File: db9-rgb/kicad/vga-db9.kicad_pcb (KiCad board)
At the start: 2 copper layers, 95 x 75 mm, 67 parts, among them J1 Conn_01x03, J2 Conn_01x03, J9 Conn_01x09

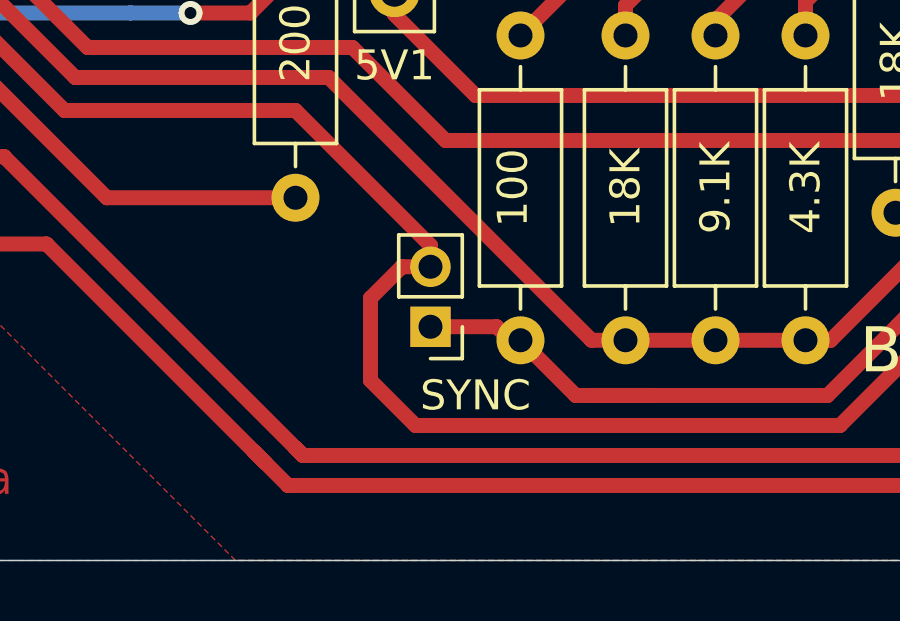
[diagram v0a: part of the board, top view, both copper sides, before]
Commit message: fix JP1 size
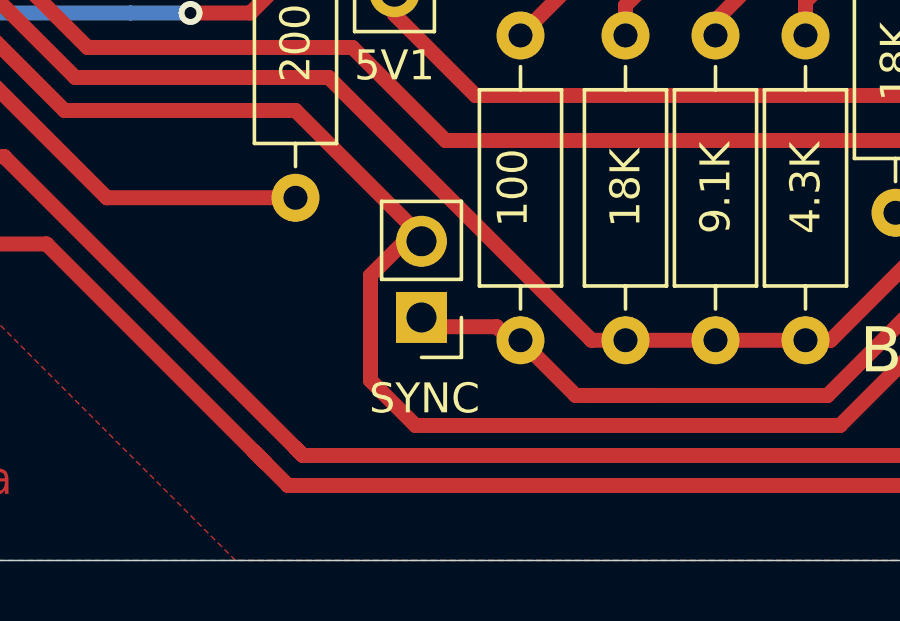
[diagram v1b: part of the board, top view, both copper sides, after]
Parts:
- JP1: footprint Connector_PinHeader_2.00mm:PinHeader_1x02_P2.00mm_Vertical -> Connector_PinHeader_2.54mm:PinHeader_1x02_P2.54mm_Vertical
- moved JP1 0.43 mm to (144.7, 121.9)
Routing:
- net Net-(HSYNC1-Pad2): track 156.5 -> 157.0 mm

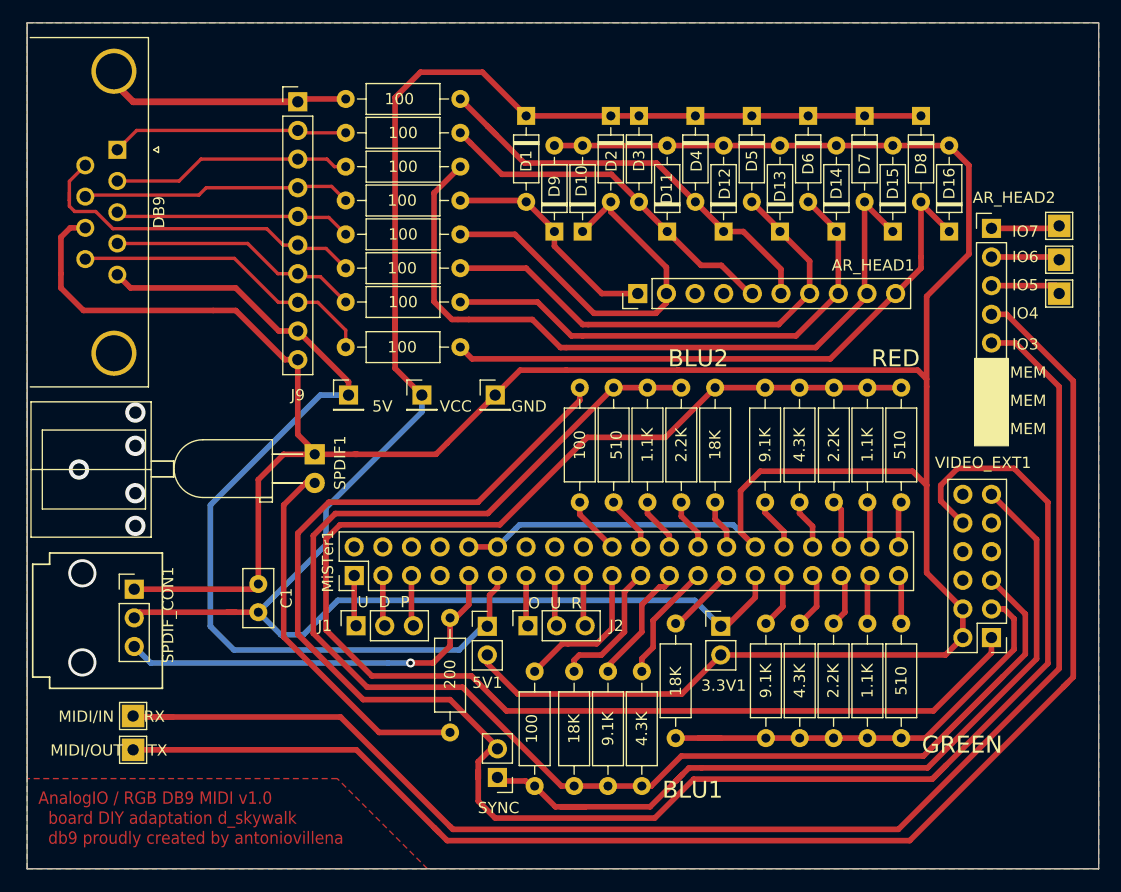
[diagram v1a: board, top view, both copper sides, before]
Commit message: update sync / new tv switch connector
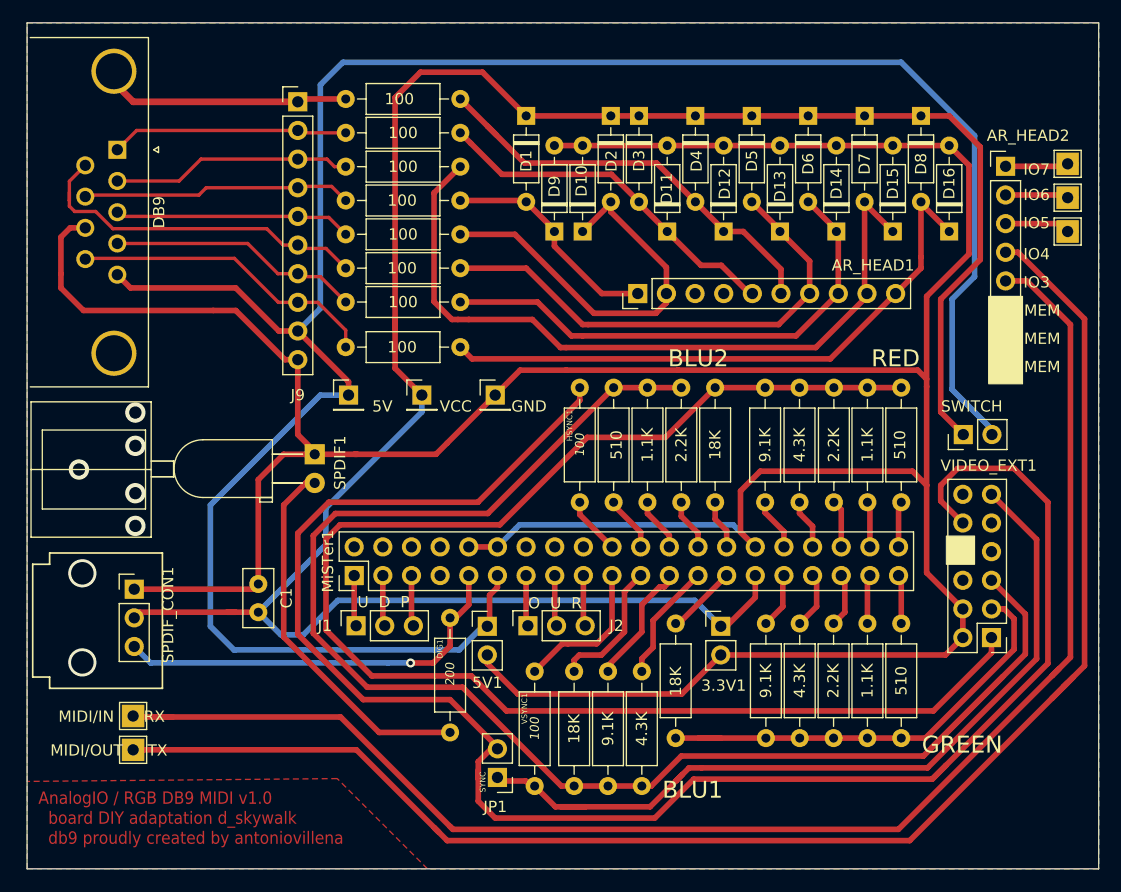
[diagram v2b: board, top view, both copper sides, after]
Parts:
- added SWITCH: PinHeader_1x02_P2.54mm_Vertical, Connector_PinHeader_2.54mm:PinHeader_1x02_P2.54mm_Vertical, F.Cu at (186.0, 91.5)
- moved AR_HEAD2 5.64 mm to (189.8, 67.7)
- moved I2S 5.55 mm to (195.2, 73.5)
- moved I2S 5.55 mm to (195.2, 70.5)
- moved I2S 5.55 mm to (195.2, 67.5)
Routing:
- net 5V: track 83.4 -> 196.4 mm
- net VCC: track 164.4 -> 198.6 mm
- net (no net): track 276.4 -> 291.8 mm

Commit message: fixed resistors and spdif.
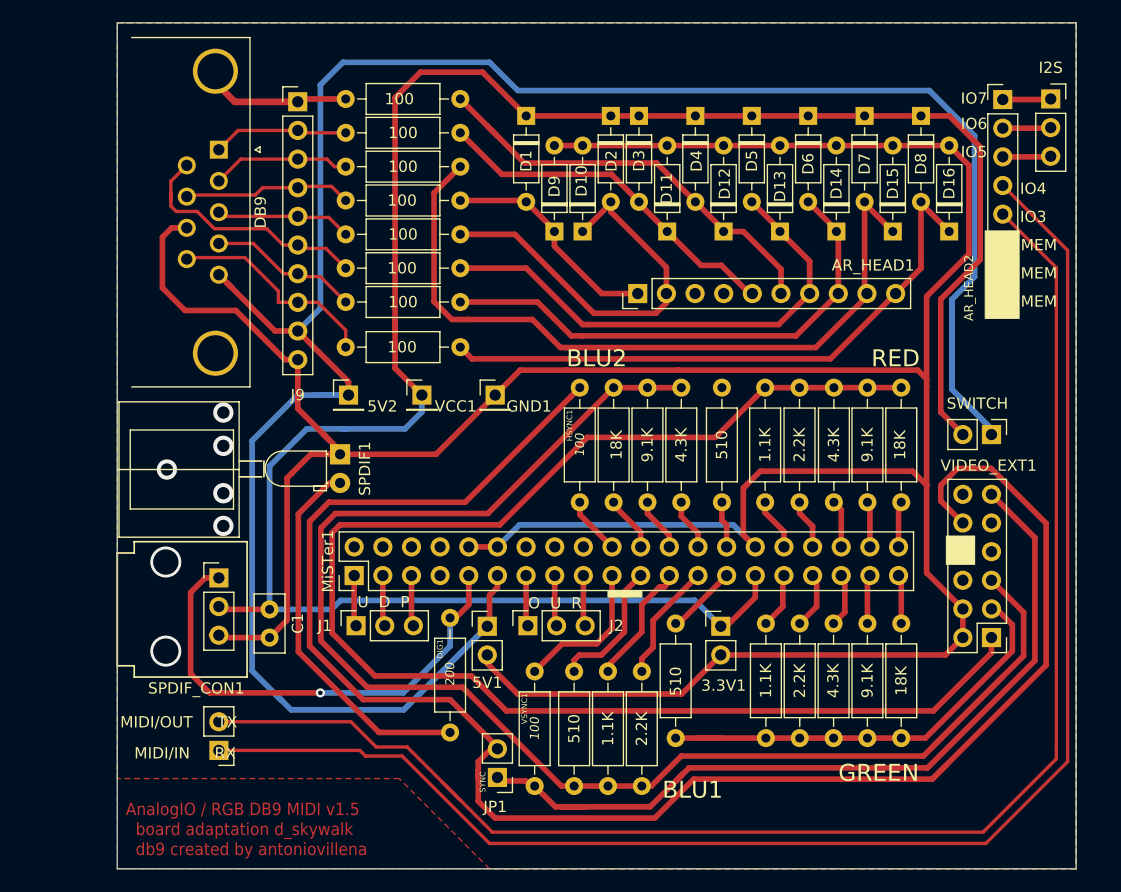
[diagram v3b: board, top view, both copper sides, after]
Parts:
- removed 5V: 5V, Connector_PinHeader_2.54mm:PinHeader_1x01_P2.54mm_Vertical
- removed the I2S at (195.2, 73.5)
- removed the I2S at (195.2, 70.5)
- removed the I2S at (195.2, 67.5)
- removed MIDI/IN      RX: TestPoint_THTPad_2.0x2.0mm_Drill1.0mm, TestPoint:TestPoint_THTPad_2.0x2.0mm_Drill1.0mm
- removed MIDI/OUT     TX: TestPoint_THTPad_2.0x2.0mm_Drill1.0mm, TestPoint:TestPoint_THTPad_2.0x2.0mm_Drill1.0mm
- added 5V2: 5V, Connector_PinHeader_2.54mm:PinHeader_1x01_P2.54mm_Vertical, F.Cu at (131.5, 88.0)
- added I2S: Conn_I2S, Connector_PinSocket_2.54mm:PinSocket_1x03_P2.54mm_Vertical, F.Cu at (193.8, 61.8)
- added MIDI: SYNC, Connector_PinHeader_2.54mm:PinHeader_1x02_P2.54mm_Vertical, F.Cu at (120.0, 119.5)
- BLU_1, GRE_1, RED_1: value 510 -> 18K
- BLU_2, GRE_2, RED_2: value 1.1K -> 9.1K
- BLU_3, GRE_3, RED_3: value 2.2K -> 4.3K
- BLU_4, GRE_4, RED_4: value 4.3K -> 2.2K
- BLU_5, GRE_5, RED_5: value 9.1K -> 1.1K
- BLU_6, GRE_6, RED_6: value 18K -> 510
- SPDIF1: footprint LED_THT:LED_D5.0mm_Horizontal_O3.81mm_Z3.0mm -> LED_THT:LED_D3.0mm_Horizontal_O1.27mm_Z2.0mm
- SWITCH: value PinHeader_1x02_P2.54mm_Vertical -> SYNC
- moved DB9 9.00 mm to (120.0, 66.2)
- moved SPDIF_CON1 7.57 mm to (120.0, 104.2)
- moved AR_HEAD2 5.93 mm to (189.5, 61.8)
- moved SWITCH 2.50 mm to (188.5, 91.5), turned to 270 degrees
- moved C1 2.46 mm to (124.5, 107.0)
- moved SPDIF1 2.25 mm to (130.8, 93.2)
- moved RED_6 0.60 mm to (164.6, 97.5)
- renumbered GND to GND1, VCC to VCC1
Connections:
- AR_HEAD2 pad 1: (no net) -> I2S-IO7
- AR_HEAD2 pad 2: (no net) -> I2S-IO6
- AR_HEAD2 pad 3: (no net) -> I2S-IO5
- AR_HEAD2 pad 4: (no net) -> MIDI-IN-RX
- AR_HEAD2 pad 5: (no net) -> MIDI-OUT-TX
- C1 pad 1: GND -> VCC
- C1 pad 2: VCC -> GND
- SPDIF_CON1 pad 1: GND -> SPDIFF
- SPDIF_CON1 pad 3: SPDIFF -> GND
- SWITCH pad 1: VCC -> 5V
- SWITCH pad 2: 5V -> VCC
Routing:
- net (no net): track 291.8 -> 0.00 mm
- net MIDI-IN-RX: track 0.00 -> 135.1 mm
- net MIDI-OUT-TX: track 0.00 -> 133.5 mm
- net GND: track 303.4 -> 292.6 mm
- net UP-DAT: track 21.0 -> 12.0 mm
- net SELECT-LAT: track 24.0 -> 15.0 mm
- net RIGHT: track 22.4 -> 13.4 mm
- net MUX: track 22.4 -> 13.4 mm
- net DOWN: track 21.3 -> 12.3 mm
- net FIRE1: track 31.7 -> 22.7 mm
- net FIRE2: track 27.3 -> 19.0 mm
- net LEFT-CLK: track 20.3 -> 12.1 mm
- net SPDIFF: track 36.7 -> 43.4 mm
- net VCC: track 198.6 -> 193.3 mm
- net I2S-IO7: track 0.00 -> 4.52 mm
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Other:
- board size 95 x 75 mm -> 85 x 75 mm
- board text added: "AnalogIO / RGB DB9 MIDI v1.5 board adaptation d_skywalk db9 created by antoniovillena"
- board text added: "MIDI/IN RX"
- board text added: "MIDI/OUT TX"
- board text removed: "AnalogIO / RGB DB9 MIDI v1.0 board DIY adaptation d_skywalk db9 proudly created by antoniovillena"

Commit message: upgraded to 1.6 - removed midi old, now using db9
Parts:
- removed AR_HEAD2: 10, Connector_PinHeader_2.54mm:PinHeader_1x08_P2.54mm_Vertical
- removed I2S: Conn_I2S, Connector_PinSocket_2.54mm:PinSocket_1x03_P2.54mm_Vertical
- removed MIDI: SYNC, Connector_PinHeader_2.54mm:PinHeader_1x02_P2.54mm_Vertical
- moved DB9_5 15.8 mm to (131.3, 61.0)
- moved DB9_6 15.8 mm to (131.2, 64.0)
- moved DB9_3 15.0 mm to (131.2, 79.8)
- moved DB9_4 15.0 mm to (131.2, 76.8)
- moved DB9_1 0.75 mm to (131.2, 70.0)
- moved DB9_2 0.75 mm to (131.2, 73.0)
- moved DB9_7 0.75 mm to (131.2, 67.0)
- renumbered SWITCH to SWITCH1
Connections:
- DB9_3 pad 1: UP-DAT -> RIGHT
- DB9_4 pad 1: MUX -> FIRE1
- DB9_5 pad 1: FIRE1 -> MUX
- DB9_6 pad 1: RIGHT -> UP-DAT
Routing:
- net MIDI-IN-RX: track 135.1 -> 0.00 mm
- net MIDI-OUT-TX: track 133.5 -> 0.00 mm
- net /AH12-IO13: track 32.0 -> 51.8 mm
- net /AF15-IO10: track 45.8 -> 55.7 mm
- net /AH11-IO12: track 38.2 -> 44.9 mm
- net I2S-IO7: track 4.52 -> 0.00 mm
- net I2S-IO6: track 4.52 -> 0.00 mm
- net I2S-IO5: track 4.52 -> 0.00 mm
- net /AG16-IO11: track 44.7 -> 40.8 mm
- net VCC: track 193.3 -> 195.7 mm
- net /AE15-IO9: track 66.9 -> 68.6 mm
- net MUX: track 13.4 -> 14.1 mm
- net (no net): vias 7 -> 11
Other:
- board size 85 x 75 mm -> 84 x 72 mm
- board text added: "AnalogIO / RGB DB9 v1.6 db9 by antoniovillena board adaptation d_skywalk"
- board text added: "H+V"
- board text added: "IO08 FIRE2"
- board text added: "IO09 DOWN"
- board text added: "IO10 UP"
- board text added: "IO11 SHIELD"
- board text added: "IO12 FIRE1"
- board text added: "IO13 RIGHT"
- board text added: "IO14 LEFT"
- board text added: "IO15 SELECT"
- board text added: "VGA/RGB"
- board text removed: "AnalogIO / RGB DB9 MIDI v1.5 board adaptation d_skywalk db9 created by antoniovillena"
- board text removed: "IO3"
- board text removed: "IO4"
- board text removed: "IO5"
- board text removed: "IO6"
- board text removed: "IO7"
- board text removed: "MEM"
- board text removed: "MIDI/IN RX"
- board text removed: "MIDI/OUT TX"

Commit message: changed AR_HEAD order
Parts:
- added G***: LOGO, componentes:logo, F.Cu at (188.5, 85.5)
- DB9 / JOY: renamed from DB9
- moved D16 35.2 mm to (149.5, 73.5)
- moved D8 35.2 mm to (147.0, 63.2)
- moved D1 34.8 mm to (182.0, 63.2)
- moved D9 34.8 mm to (184.5, 73.5)
- moved D15 25.2 mm to (154.5, 73.5)
- moved D7 25.2 mm to (152.0, 63.2)
- moved D10 24.8 mm to (177.0, 73.5)
- moved D2 24.8 mm to (179.5, 63.2)
- moved AR_HEAD 22.9 mm to (180.0, 79.0), turned to 270 degrees
- moved D14 15.2 mm to (159.5, 73.5)
- moved D6 15.2 mm to (157.0, 63.2)
- moved D11 14.8 mm to (174.5, 73.5)
- moved D3 14.8 mm to (172.0, 63.2)
- moved D13 5.25 mm to (164.5, 73.5)
- moved D5 5.25 mm to (162.0, 63.2)
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- renumbered VCC1 to 3.3V, 3.3V1 to 3.3V, 5V2 to 5V, 5V1 to 5V, AR_HEAD1 to AR_HEAD, GND1 to GND, MiSTer1 to MiSTer, SPDIF1 to SPDIF, SWITCH1 to SWITCH, VIDEO_EXT1 to VIDEO_EXT
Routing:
- net /AG11-IO15: track 20.5 -> 75.5 mm
- net /AE15-IO9: track 68.6 -> 24.7 mm
- net /AH9-IO14: track 37.1 -> 65.0 mm
- net /AF15-IO10: track 55.7 -> 28.6 mm
- net /AF17-IO8: track 54.1 -> 33.5 mm
- net /AH12-IO13: track 51.8 -> 42.3 mm
- net /AG16-IO11: track 40.8 -> 33.8 mm
- net /AH11-IO12: track 44.9 -> 39.2 mm
- net Net-(DIG1-Pad2): track 32.5 -> 33.5 mm
- net VCC: track 195.7 -> 194.9 mm
- net GND: track 292.6 -> 292.2 mm, vias 0 -> 21
- net (no net): vias 11 -> 5
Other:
- outline, holes or cut-outs redrawn
- board text added: "AREF N/C"
- board text added: "GND N/C"
- board text added: "SCL SELECT"
- board text added: "SDA LEFT"
- board text added: "VCC"
- board text removed: "IO14 LEFT"
- board text removed: "IO15 SELECT"
